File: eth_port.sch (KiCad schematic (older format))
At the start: 0 parts

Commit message: - Created QFN72 footprint for LAN8810 chip - Started basic schematic power bypassing - Imported into layout to get an initial look
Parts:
- added C201, C202, C203, C204, C205, C206, C207, C208, C209, C210, C211, C212, C213, C214, C215, C216: 10n, Capacitor_SMD:C_0603_1608Metric, symbol Device:C
- added R201: 8.06k, Resistor_SMD:R_0603_1608Metric, symbol Device:R_US
- added U201: LAN8810, myfp:QFN-72-1EP_10x10mm_P0.5mm_EP6x6mm_ThermalVias, symbol mysyms:LAN8810
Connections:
- new net: C205.1, C207.1, C209.1, C211.1, C213.1, C215.1, U201.14 (VDDVARIO), U201.23 (VDDVARIO), U201.32 (VDDVARIO), U201.41 (VDDVARIO), U201.49 (VDDVARIO), U201.6 (VDDVARIO)
- new net: C206.1, C208.1, C210.1, C212.1, C214.1, C216.1, U201.15 (VDD12CORE), U201.24 (VDD12CORE), U201.31 (VDD12CORE), U201.40 (VDD12CORE), U201.48 (VDD12CORE), U201.7 (VDD12CORE)
- new net: R201.1, U201.54 (ETHRBIAS)
- new net: C201.1, C202.1, C203.1, C204.1, U201.59 (VDD12A), U201.62 (VDD12A), U201.67 (VDD12A), U201.70 (VDD12A)
- new net GND: C201.2, C202.2, C203.2, C204.2, C205.2, C206.2, C207.2, C208.2, C209.2, C210.2, C211.2, C212.2, C213.2, C214.2, C215.2, C216.2, R201.2, U201.PAD (VSS)
- new net RXD0: U201.8 (RXD0)
- new net RXD1: U201.9 (RXD1)
- new net RXD2: U201.10 (RXD2)
- new net RXD3: U201.11 (RXD3)
- new net RXD4: U201.12 (RXD4)
- new net RXD5: U201.13 (RXD5)
- new net RXD6: U201.16 (RXD6)
- new net RXD7: U201.17 (RXD7)
- new net TXD0: U201.35 (TXD0)
- new net TXD1: U201.34 (TXD1)
- new net TXD2: U201.33 (TXD2)
- new net TXD3: U201.30 (TXD3)
- new net TXD4: U201.29 (TXD4)
- new net TXD5: U201.28 (TXD5)
- new net TXD6: U201.27 (TXD6)
- new net TXD7: U201.26 (TXD7)

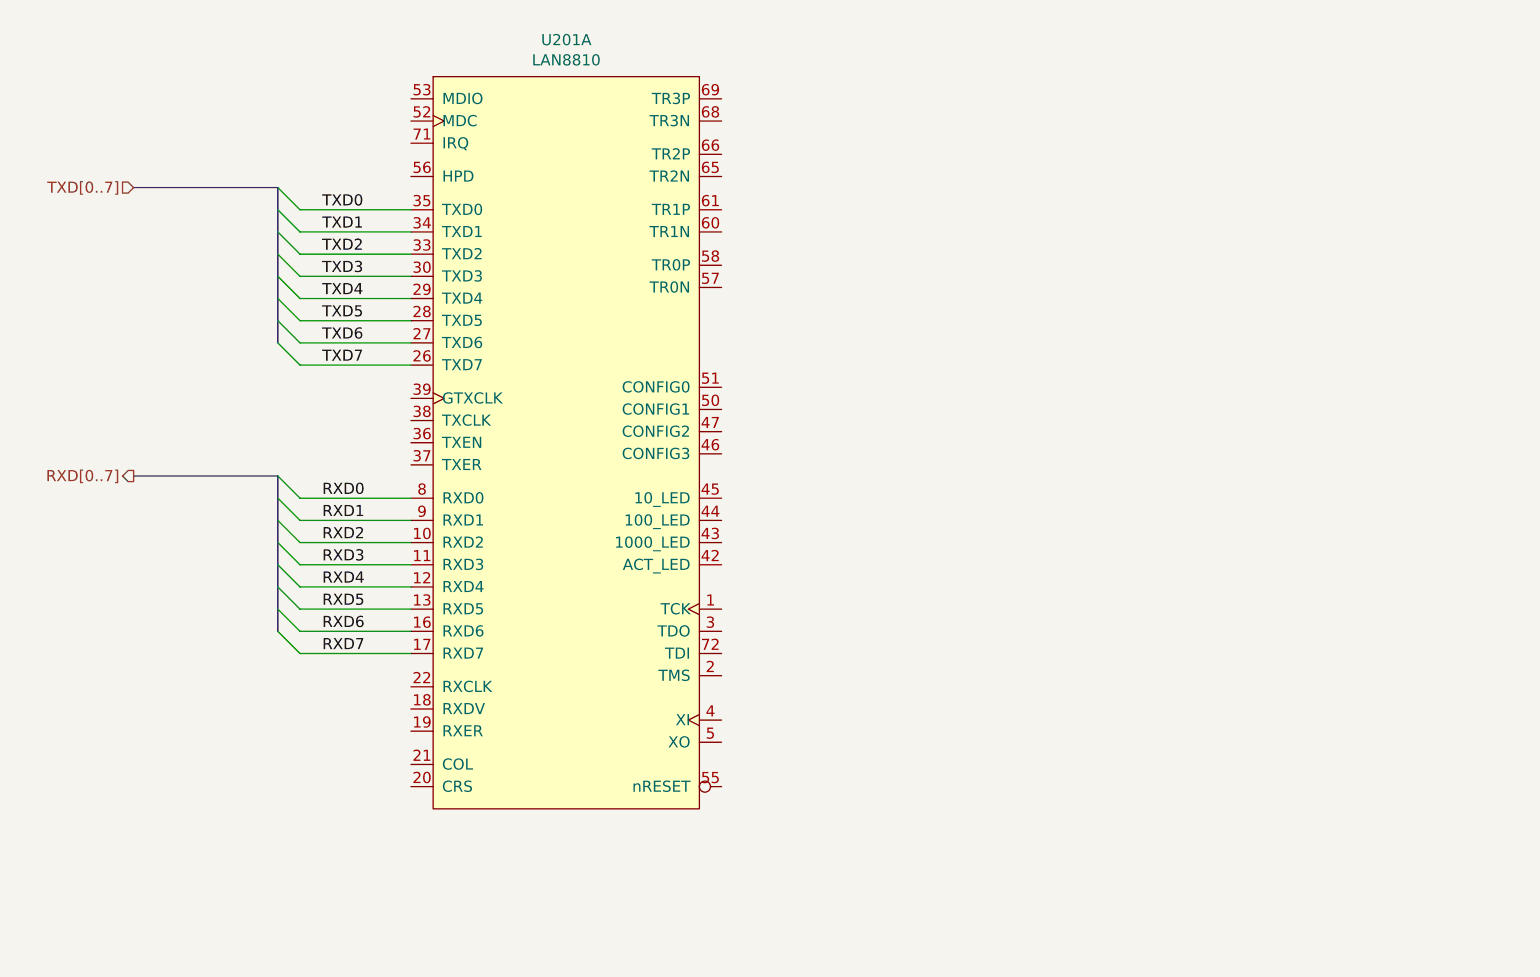
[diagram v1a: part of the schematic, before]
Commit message: - Picked a GigE transformer - Created schematic symbol & footprint for it - Added to design with bare hookup to PHY
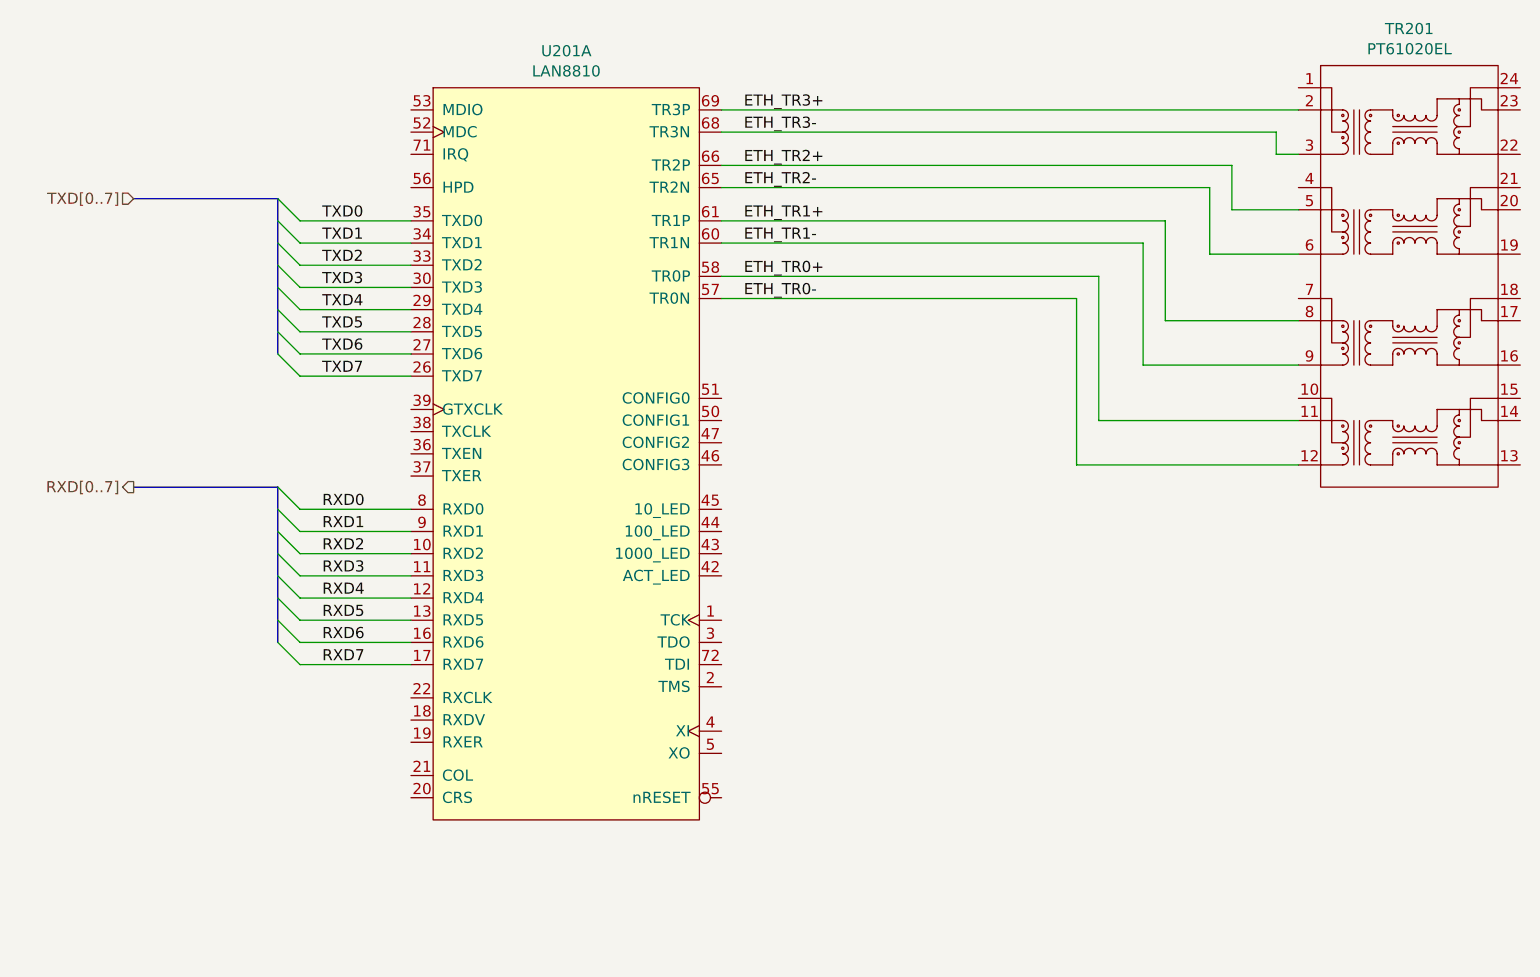
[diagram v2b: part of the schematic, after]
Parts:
- added TR201: PT61020EL, myfp:magnetics_PT61020E, symbol mysyms:PT61020EL
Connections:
- net ETH_TR0-: now reaches U201.57 (TR0N)
- net ETH_TR0-: now also TR201.12 (TD4-)
- net ETH_TR0+: now reaches U201.58 (TR0P)
- net ETH_TR0+: now also TR201.11 (TD4+)
- net ETH_TR1-: now reaches U201.60 (TR1N)
- net ETH_TR1-: now also TR201.9 (TD3-)
- net ETH_TR1+: now reaches U201.61 (TR1P)
- net ETH_TR1+: now also TR201.8 (TD3+)
- net ETH_TR2-: now reaches U201.65 (TR2N)
- net ETH_TR2-: now also TR201.6 (TD2-)
- net ETH_TR2+: now reaches U201.66 (TR2P)
- net ETH_TR2+: now also TR201.5 (TD2+)
- net ETH_TR3-: now reaches U201.68 (TR3N)
- net ETH_TR3-: now also TR201.3 (TD1-)
- net ETH_TR3+: now reaches U201.69 (TR3P)
- net ETH_TR3+: now also TR201.2 (TD1+)
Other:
- moved on the sheet: U201A
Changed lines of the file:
@@
 L mysyms:LAN8810 U201
 U 1 1 638E63D5
-P 4500 2700
-F 0 "U201" H 4500 4515 50  0000 C CNN
-F 1 "LAN8810" H 4500 4424 50  0000 C CNN
-F 2 "myfp:QFN-72-1EP_10x10mm_P0.5mm_EP6x6mm_ThermalVias" H 4500 2700 50  0001 C CNN
-F 3 "" H 4500 2700 50  0001 C CNN
-	1    4500 2700
+P 4500 2750
+F 0 "U201" H 4500 4565 50  0000 C CNN
+F 1 "LAN8810" H 4500 4474 50  0000 C CNN
+F 2 "myfp:QFN-72-1EP_10x10mm_P0.5mm_EP6x6mm_ThermalVias" H 4500 2750 50  0001 C CNN
+F 3 "" H 4500 2750 50  0001 C CNN
+	1    4500 2750
 	1    0    0    -1
 $EndComp
@@
 Connection ~ 7200 7950
 Wire Bus Line
-	2550 2850 3200 2850
-Wire Wire Line
-	3800 2950 3300 2950
-Text Label 3400 2950 0    50   ~ 0
+	2550 2900 3200 2900
+Wire Wire Line
+	3800 3000 3300 3000
+Text Label 3400 3000 0    50   ~ 0
 RXD0
 Wire Wire Line
-	3800 3050 3300 3050
-Wire Wire Line
-	3800 3150 3300 3150
-Wire Wire Line
-	3800 3250 3300 3250
-Wire Wire Line
-	3800 3350 3300 3350
-Wire Wire Line
-	3800 3450 3300 3450
-Wire Wire Line
-	3800 3550 3300 3550
-Wire Wire Line
-	3800 3650 3300 3650
-Text Label 3400 3050 0    50   ~ 0
+	3800 3100 3300 3100
+Wire Wire Line
+	3800 3200 3300 3200
+Wire Wire Line
+	3800 3300 3300 3300
+Wire Wire Line
+	3800 3400 3300 3400
+Wire Wire Line
+	3800 3500 3300 3500
+Wire Wire Line
+	3800 3600 3300 3600
+Wire Wire Line
+	3800 3700 3300 3700
+Text Label 3400 3100 0    50   ~ 0
 RXD1
-Text Label 3400 3150 0    50   ~ 0
+Text Label 3400 3200 0    50   ~ 0
 RXD2
-Text Label 3400 3250 0    50   ~ 0
+Text Label 3400 3300 0    50   ~ 0
 RXD3
-Text Label 3400 3350 0    50   ~ 0
+Text Label 3400 3400 0    50   ~ 0
 RXD4
-Text Label 3400 3450 0    50   ~ 0
+Text Label 3400 3500 0    50   ~ 0
 RXD5
-Text Label 3400 3550 0    50   ~ 0
+Text Label 3400 3600 0    50   ~ 0
 RXD6
-Text Label 3400 3650 0    50   ~ 0
+Text Label 3400 3700 0    50   ~ 0
 RXD7
 Entry Wire Line
-	3200 2850 3300 2950
-Entry Wire Line
-	3200 2950 3300 3050
-Entry Wire Line
-	3200 3050 3300 3150
-Entry Wire Line
-	3200 3150 3300 3250
-Entry Wire Line
-	3200 3250 3300 3350
-Entry Wire Line
-	3200 3350 3300 3450
-Entry Wire Line
-	3200 3450 3300 3550
-Entry Wire Line
-	3200 3550 3300 3650
+	3200 2900 3300 3000
+Entry Wire Line
+	3200 3000 3300 3100
+Entry Wire Line
+	3200 3100 3300 3200
+Entry Wire Line
+	3200 3200 3300 3300
+Entry Wire Line
+	3200 3300 3300 3400
+Entry Wire Line
+	3200 3400 3300 3500
+Entry Wire Line
+	3200 3500 3300 3600
+Entry Wire Line
+	3200 3600 3300 3700
 Wire Bus Line
-	2550 1550 3200 1550
-Wire Wire Line
-	3800 1650 3300 1650
-Text Label 3400 1650 0    50   ~ 0
+	2550 1600 3200 1600
+Wire Wire Line
+	3800 1700 3300 1700
+Text Label 3400 1700 0    50   ~ 0
 TXD0
 Wire Wire Line
-	3800 1750 3300 1750
-Wire Wire Line
-	3800 1850 3300 1850
-Wire Wire Line
-	3800 1950 3300 1950
-Wire Wire Line
-	3800 2050 3300 2050
-Wire Wire Line
-	3800 2150 3300 2150
-Wire Wire Line
-	3800 2250 3300 2250
-Wire Wire Line
-	3800 2350 3300 2350
-Text Label 3400 1750 0    50   ~ 0
+	3800 1800 3300 1800
+Wire Wire Line
+	3800 1900 3300 1900
+Wire Wire Line
+	3800 2000 3300 2000
+Wire Wire Line
+	3800 2100 3300 2100
+Wire Wire Line
+	3800 2200 3300 2200
+Wire Wire Line
+	3800 2300 3300 2300
+Wire Wire Line
+	3800 2400 3300 2400
+Text Label 3400 1800 0    50   ~ 0
 TXD1
-Text Label 3400 1850 0    50   ~ 0
+Text Label 3400 1900 0    50   ~ 0
 TXD2
-Text Label 3400 1950 0    50   ~ 0
+Text Label 3400 2000 0    50   ~ 0
 TXD3
-Text Label 3400 2050 0    50   ~ 0
+Text Label 3400 2100 0    50   ~ 0
 TXD4
-Text Label 3400 2150 0    50   ~ 0
+Text Label 3400 2200 0    50   ~ 0
 TXD5
-Text Label 3400 2250 0    50   ~ 0
+Text Label 3400 2300 0    50   ~ 0
 TXD6
-Text Label 3400 2350 0    50   ~ 0
+Text Label 3400 2400 0    50   ~ 0
 TXD7
 Entry Wire Line
-	3200 1550 3300 1650
-Entry Wire Line
-	3200 1650 3300 1750
-Entry Wire Line
-	3200 1750 3300 1850
-Entry Wire Line
-	3200 1850 3300 1950
-Entry Wire Line
-	3200 1950 3300 2050
-Entry Wire Line
-	3200 2050 3300 2150
-Entry Wire Line
-	3200 2150 3300 2250
-Entry Wire Line
-	3200 2250 3300 2350
-Text HLabel 2550 2850 0    50   Output ~ 0
+	3200 1600 3300 1700
+Entry Wire Line
+	3200 1700 3300 1800
+Entry Wire Line
+	3200 1800 3300 1900
+Entry Wire Line
+	3200 1900 3300 2000
+Entry Wire Line
+	3200 2000 3300 2100
+Entry Wire Line
+	3200 2100 3300 2200
+Entry Wire Line
+	3200 2200 3300 2300
+Entry Wire Line
+	3200 2300 3300 2400
+Text HLabel 2550 2900 0    50   Output ~ 0
 RXD[0..7]
-Text HLabel 2550 1550 0    50   Input ~ 0
+Text HLabel 2550 1600 0    50   Input ~ 0
 TXD[0..7]
+$Comp
+L mysyms:PT61020EL TR201
+U 1 1 638F89C6
+P 8300 1950
+F 0 "TR201" H 8300 3065 50  0000 C CNN
+F 1 "PT61020EL" H 8300 2974 50  0000 C CNN
+F 2 "myfp:magnetics_PT61020E" H 8300 950 50  0001 C CNN
+F 3 "" H 8300 1950 50  0001 C CNN
+	1    8300 1950
+	1    0    0    -1
+$EndComp
+Wire Wire Line
+	7800 1200 5200 1200
+Wire Wire Line
+	7800 1400 7700 1400
+Wire Wire Line
+	7700 1400 7700 1300
+Wire Wire Line
+	5200 1300 7700 1300
+Wire Wire Line
+	7800 2150 7200 2150
+Wire Wire Line
+	7200 2150 7200 1700
+Wire Wire Line
+	7200 1700 5200 1700
+Wire Wire Line
+	7400 1850 7400 1550
+Wire Wire Line
+	7400 1850 7800 1850
+Wire Wire Line
+	7400 1550 5200 1550
+Wire Wire Line
+	7500 1650 7500 1450
+Wire Wire Line
+	7500 1650 7800 1650
+Wire Wire Line
+	7500 1450 5200 1450
+Wire Wire Line
+	7800 2350 7100 2350
+Wire Wire Line
+	7100 2350 7100 1800
+Wire Wire Line
+	7100 1800 5200 1800
+Wire Wire Line
+	7800 2600 6900 2600
+Wire Wire Line
+	6900 2600 6900 1950
+Wire Wire Line
+	6900 1950 5200 1950
+Wire Wire Line
+	7800 2800 6800 2800
+Wire Wire Line
+	6800 2800 6800 2050
+Wire Wire Line
+	6800 2050 5200 2050
 Wire Bus Line
-	3200 2850 3200 3550
+	3200 2900 3200 3600
 Wire Bus Line
-	3200 1550 3200 2250
+	3200 1600 3200 2300
+Text Label 5300 1200 0    50   ~ 0
+ETH_TR3+
+Text Label 5300 1300 0    50   ~ 0
+ETH_TR3-
+Text Label 5300 1450 0    50   ~ 0
+ETH_TR2+
+Text Label 5300 1550 0    50   ~ 0
+ETH_TR2-
+Text Label 5300 1700 0    50   ~ 0
+ETH_TR1+
+Text Label 5300 1800 0    50   ~ 0
+ETH_TR1-
+Text Label 5300 1950 0    50   ~ 0
+ETH_TR0+
+Text Label 5300 2050 0    50   ~ 0
+ETH_TR0-
 $EndSCHEMATC
